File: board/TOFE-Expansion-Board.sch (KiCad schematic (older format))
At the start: 6 parts, among them U1 TOFE-8X, U7 24AA01/24LC01B

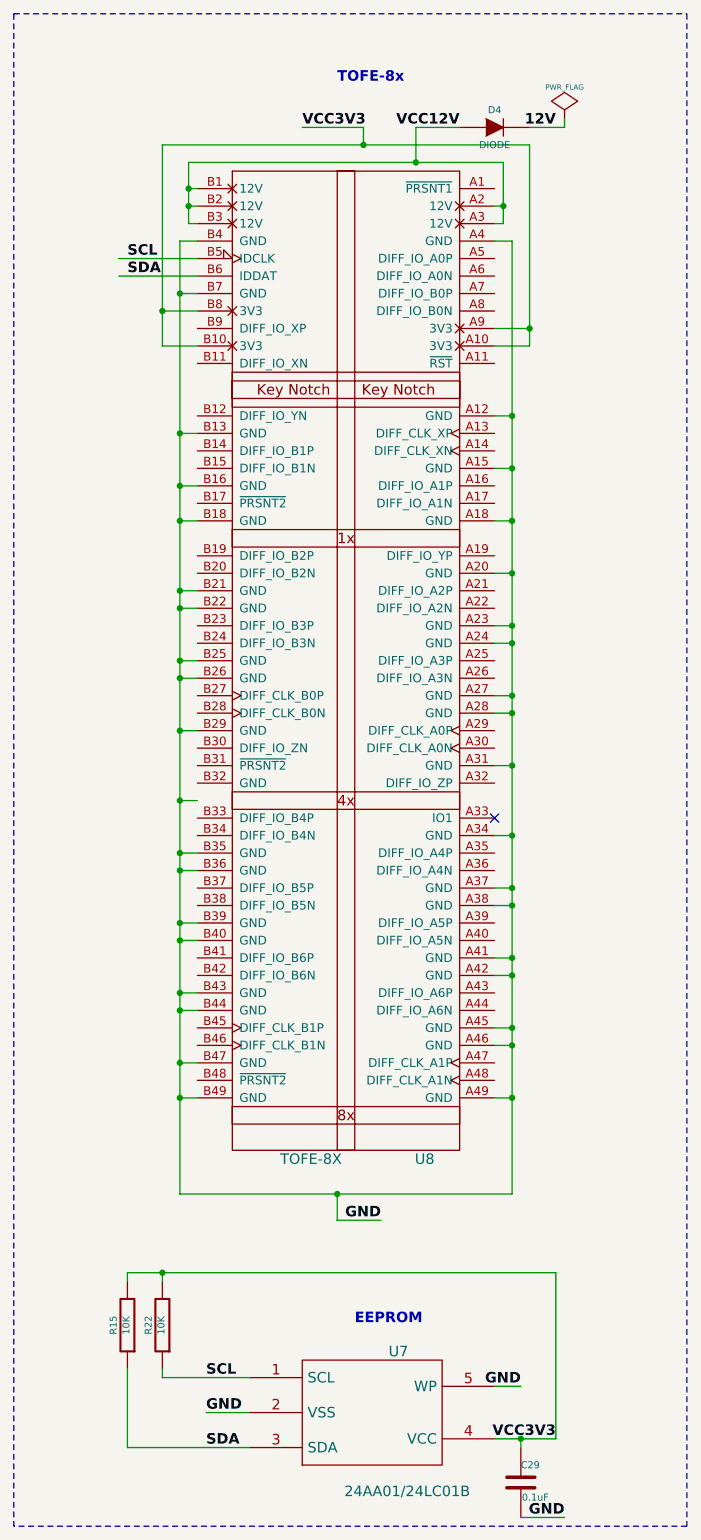
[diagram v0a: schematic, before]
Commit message: schematic: Fixing GND alignment after last change.
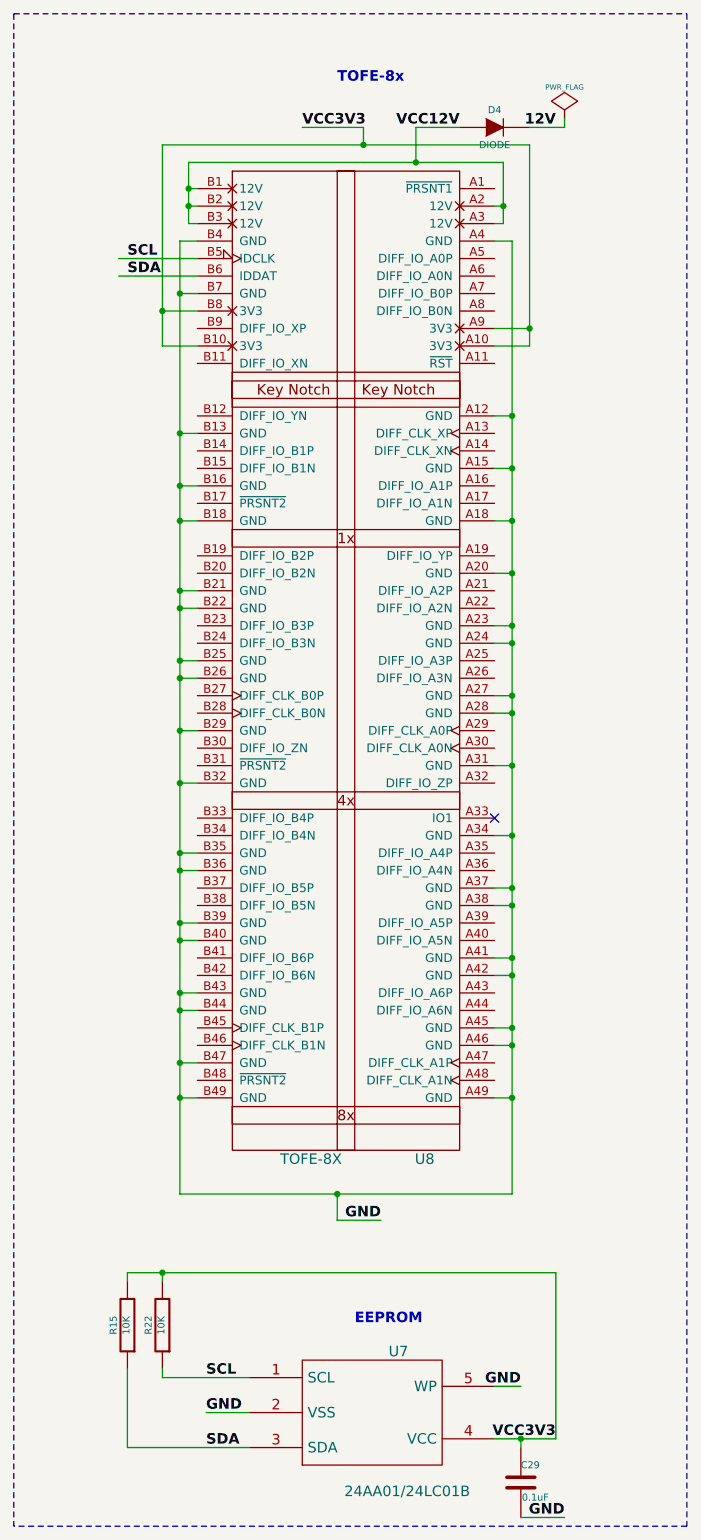
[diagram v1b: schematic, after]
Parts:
- renumbered U1 to U8
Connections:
- wire segments 78 -> 123
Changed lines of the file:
@@
 Sheet 1 1
 Title "TOFE Expansion Board"
-Date "15 oct 2015"
+Date "29 oct 2015"
 Rev "1.0"
 Comp "Numato Lab"
@@
 $EndDescr
 $Comp
-L TOFE-8X U1
+L TOFE-8X U8
 U 1 1 561CABB0
 P 5450 5200
@@
 	4150 2800 4050 2800
 Wire Wire Line
-	4050 2800 4050 8250
+	4050 2800 4050 3100
+Wire Wire Line
+	4050 3100 4050 3900
+Wire Wire Line
+	4050 3900 4050 4200
+Wire Wire Line
+	4050 4200 4050 4400
+Wire Wire Line
+	4050 4400 4050 4800
+Wire Wire Line
+	4050 4800 4050 4900
+Wire Wire Line
+	4050 4900 4050 5200
+Wire Wire Line
+	4050 5200 4050 5300
+Wire Wire Line
+	4050 5300 4050 5600
+Wire Wire Line
+	4050 5600 4050 5900
+Wire Wire Line
+	4050 5900 4050 6300
+Wire Wire Line
+	4050 6300 4050 6400
+Wire Wire Line
+	4050 6400 4050 6700
+Wire Wire Line
+	4050 6700 4050 6800
+Wire Wire Line
+	4050 6800 4050 7100
+Wire Wire Line
+	4050 7100 4050 7200
+Wire Wire Line
+	4050 7200 4050 7500
+Wire Wire Line
+	4050 7500 4050 7700
+Wire Wire Line
+	4050 7700 4050 8250
 Wire Wire Line
 	4050 3100 4150 3100
@@
 Connection ~ 4050 5300
 Wire Wire Line
-	4050 6000 4150 6000
+	4050 5900 4150 5900
 Connection ~ 4050 5600
 Wire Wire Line
 	4050 6300 4150 6300
-Connection ~ 4050 6000
+Connection ~ 4050 5900
 Wire Wire Line
 	4050 6400 4150 6400
@@
 Connection ~ 5950 7400
 Wire Wire Line
-	4050 8250 5950 8250
+	4050 8250 4950 8250
+Wire Wire Line
+	4950 8250 5950 8250
 Connection ~ 4050 7700
 Connection ~ 5950 7700
@@
 	3950 3400 4150 3400
 Wire Wire Line
-	3950 2250 3950 3400
+	3950 2250 3950 3200
+Wire Wire Line
+	3950 3200 3950 3400
 Wire Wire Line
 	3950 3200 4150 3200
@@
 	5850 3300 6050 3300
 Wire Wire Line
-	6050 2250 6050 3400
+	6050 2250 6050 3300
+Wire Wire Line
+	6050 3300 6050 3400
 Wire Wire Line
 	6050 3400 5850 3400
 Wire Wire Line
-	3950 2250 6050 2250
+	3950 2250 5100 2250
+Wire Wire Line
+	5100 2250 6050 2250
 Connection ~ 6050 3300
 Connection ~ 3950 3200
@@
 	4100 2700 4150 2700
 Wire Wire Line
-	4100 2350 4100 2700
+	4100 2350 4100 2500
+Wire Wire Line
+	4100 2500 4100 2600
+Wire Wire Line
+	4100 2600 4100 2700
 Wire Wire Line
 	4100 2600 4150 2600
@@
 	5900 2700 5850 2700
 Wire Wire Line
-	5900 2350 5900 2700
+	5900 2350 5900 2600
+Wire Wire Line
+	5900 2600 5900 2700
 Wire Wire Line
 	5900 2600 5850 2600
 Wire Wire Line
-	4100 2350 5900 2350
+	4100 2350 5400 2350
+Wire Wire Line
+	5400 2350 5900 2350
 Connection ~ 5900 2600
 Connection ~ 4100 2500
@@
 	6250 2150 6250 2100
 Wire Wire Line
-	5850 9650 6200 9650
+	5850 9650 6000 9650
+Wire Wire Line
+	6000 9650 6200 9650
 Wire Wire Line
 	3950 9300 3950 9250
@@
 	3750 8750 3750 8700
 Wire Wire Line
-	3750 8700 6200 8700
+	3750 8700 3950 8700
+Wire Wire Line
+	3950 8700 6200 8700
 Wire Wire Line
 	3950 8750 3950 8700
@@
 	6000 10100 6250 10100
 Wire Wire Line
-	5950 8250 5950 2800
+	5950 8250 5950 7700
+Wire Wire Line
+	5950 7700 5950 7400
+Wire Wire Line
+	5950 7400 5950 7300
+Wire Wire Line
+	5950 7300 5950 7000
+Wire Wire Line
+	5950 7000 5950 6900
+Wire Wire Line
+	5950 6900 5950 6600
+Wire Wire Line
+	5950 6600 5950 6500
+Wire Wire Line
+	5950 6500 5950 6200
+Wire Wire Line
+	5950 6200 5950 5800
+Wire Wire Line
+	5950 5800 5950 5500
+Wire Wire Line
+	5950 5500 5950 5400
+Wire Wire Line
+	5950 5400 5950 5100
+Wire Wire Line
+	5950 5100 5950 5000
+Wire Wire Line
+	5950 5000 5950 4700
+Wire Wire Line
+	5950 4700 5950 4400
+Wire Wire Line
+	5950 4400 5950 4100
+Wire Wire Line
+	5950 4100 5950 3800
+Wire Wire Line
+	5950 3800 5950 2800
 Text Label 3750 2900 0    60   ~ 12
 SCL
